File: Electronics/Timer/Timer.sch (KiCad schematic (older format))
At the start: 13 parts, among them J1 RJ12-UNSHLD, U1 74HC165

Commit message: Updated Timer schematic and updated PCB footprints
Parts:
- removed D2: D, Diodes_THT:D_A-405_P5.08mm_Vertical_AnodeUp, symbol D
- added C3: 270pF, Capacitors_SMD:C_0603_HandSoldering, symbol C
- added D2, D3, D4: D_Zener, Diodes_SMD:SOD-80C, symbol D_Zener
- added R2: 10, Resistors_SMD:R_1206_HandSoldering, symbol R
- added R3, R4: 470, Resistors_SMD:R_1206_HandSoldering, symbol R
- C1: value C -> 270pF; footprint Capacitors_THT:C_Disc_D4.3mm_W1.9mm_P5.00mm -> Capacitors_SMD:C_0603_HandSoldering
- C2: value CP1 -> 10uF; footprint Capacitors_THT:CP_Axial_L10.0mm_D6.0mm_P15.00mm_Horizontal -> Capacitors_SMD:C_1210_HandSoldering
- R1: value R -> 68; footprint Resistors_THT:R_Axial_DIN0309_L9.0mm_D3.2mm_P2.54mm_Vertical -> Resistors_SMD:R_1206_HandSoldering
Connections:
- wire segments 45 -> 57
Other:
- moved on the sheet: C2, D1, J1, R1

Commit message: Updated Timer PCB and exported GERBERS
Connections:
- net at RN1.2 (R1), U1.11 (A): now also S2.1 (Com1); no longer S1.1 (Com1)
- net at RN1.3 (R2), U1.12 (B): now also S3.1 (Com1); no longer S2.1 (Com1)
- net at RN1.4 (R3), U1.13 (C): now also S4.1 (Com1); no longer S3.1 (Com1)
- net at RN1.5 (R4), U1.14 (D): now also S5.1 (Com1); no longer S4.1 (Com1)
- net at RN1.6 (R5), U1.6 (H): now also S1.1 (Com1); no longer S5.1 (Com1)
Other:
- moved on the sheet: S1, S2, S3, S4, S5
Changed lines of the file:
@@
 L DPDT-Button S1
 U 1 1 5B2D9B30
+P 3300 5300
+F 0 "S1" H 3300 5750 60  0000 C CNN
+F 1 "DPDT-Button" H 3300 5300 60  0000 C CNN
+F 2 "PiKwonDo:Switch-DPDT" H 3300 5300 60  0001 C CNN
+F 3 "" H 3300 5300 60  0001 C CNN
+	1    3300 5300
+	1    0    0    -1
+$EndComp
+$Comp
+L DPDT-Button S2
+U 1 1 5B2D9E5E
 P 3300 1700
-F 0 "S1" H 3300 2150 60  0000 C CNN
+F 0 "S2" H 3300 2150 60  0000 C CNN
 F 1 "DPDT-Button" H 3300 1700 60  0000 C CNN
 F 2 "PiKwonDo:Switch-DPDT" H 3300 1700 60  0001 C CNN
@@
 $EndComp
 $Comp
-L DPDT-Button S2
-U 1 1 5B2D9E5E
+L DPDT-Button S3
+U 1 1 5B2D9EA4
 P 3300 2600
-F 0 "S2" H 3300 3050 60  0000 C CNN
+F 0 "S3" H 3300 3050 60  0000 C CNN
 F 1 "DPDT-Button" H 3300 2600 60  0000 C CNN
 F 2 "PiKwonDo:Switch-DPDT" H 3300 2600 60  0001 C CNN
@@
 $EndComp
 $Comp
-L DPDT-Button S3
-U 1 1 5B2D9EA4
+L DPDT-Button S4
+U 1 1 5B2D9EFB
 P 3300 3500
-F 0 "S3" H 3300 3950 60  0000 C CNN
+F 0 "S4" H 3300 3950 60  0000 C CNN
 F 1 "DPDT-Button" H 3300 3500 60  0000 C CNN
 F 2 "PiKwonDo:Switch-DPDT" H 3300 3500 60  0001 C CNN
@@
 $EndComp
 $Comp
-L DPDT-Button S4
-U 1 1 5B2D9EFB
+L DPDT-Button S5
+U 1 1 5B2D9F4B
 P 3300 4400
-F 0 "S4" H 3300 4850 60  0000 C CNN
+F 0 "S5" H 3300 4850 60  0000 C CNN
 F 1 "DPDT-Button" H 3300 4400 60  0000 C CNN
 F 2 "PiKwonDo:Switch-DPDT" H 3300 4400 60  0001 C CNN
@@
 	1    0    0    -1
 $EndComp
-$Comp
-L DPDT-Button S5
-U 1 1 5B2D9F4B
-P 3300 5300
-F 0 "S5" H 3300 5750 60  0000 C CNN
-F 1 "DPDT-Button" H 3300 5300 60  0000 C CNN
-F 2 "PiKwonDo:Switch-DPDT" H 3300 5300 60  0001 C CNN
-F 3 "" H 3300 5300 60  0001 C CNN
-	1    3300 5300
-	1    0    0    -1
-$EndComp

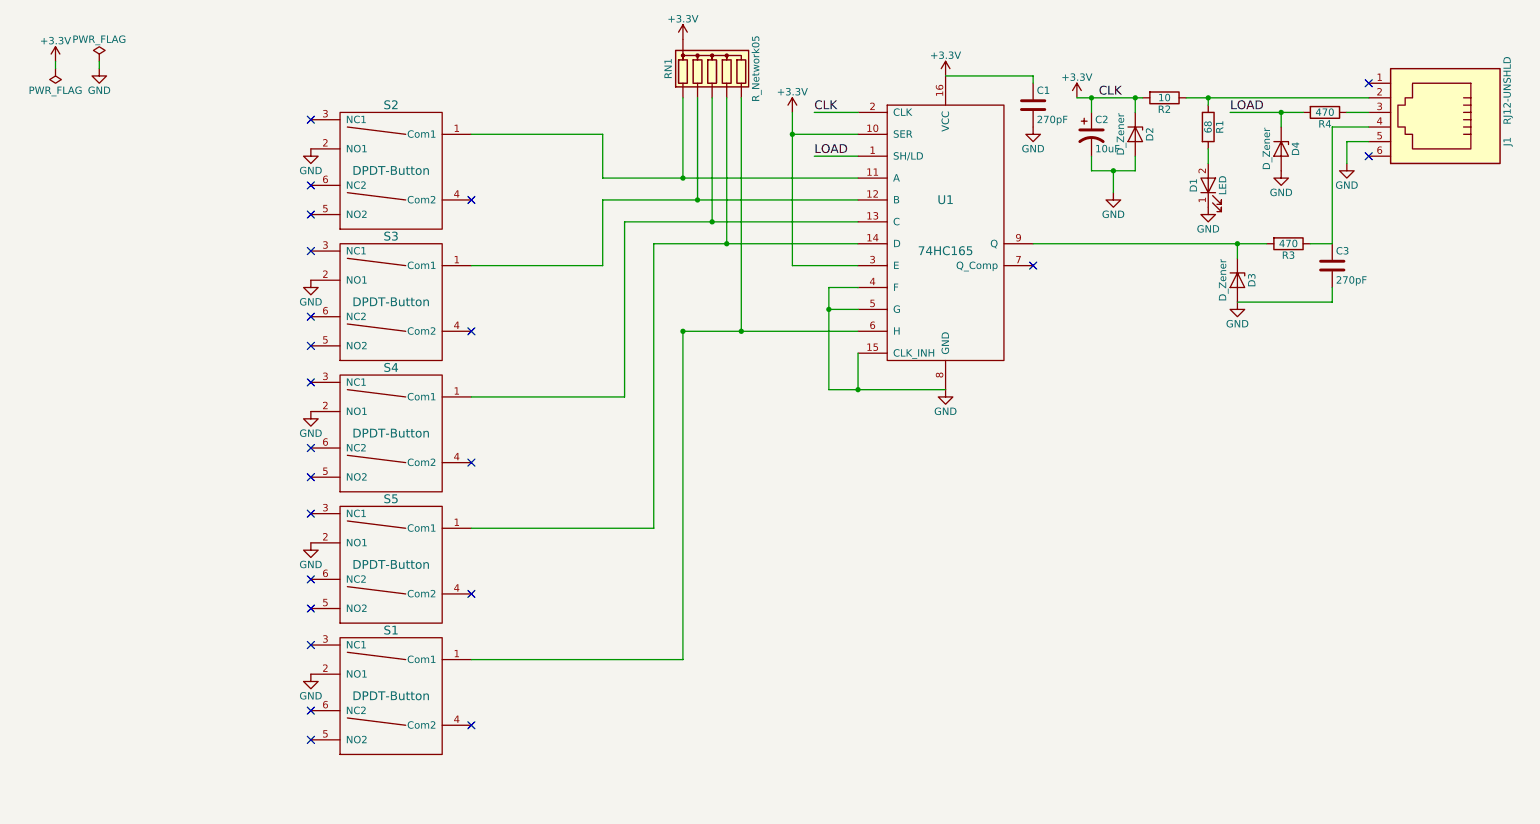
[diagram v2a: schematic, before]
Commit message: Completed HAT PCB
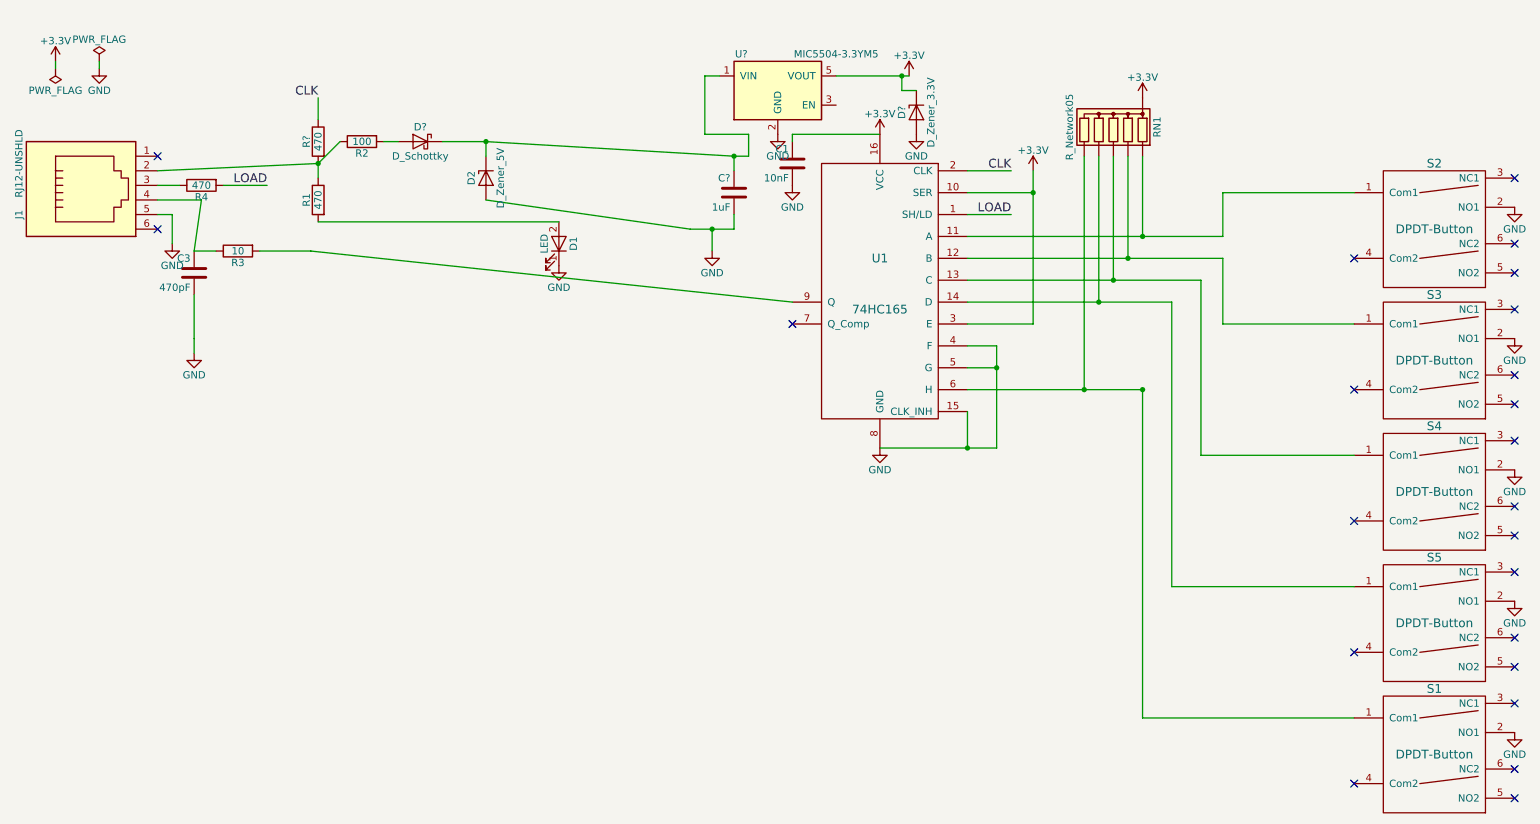
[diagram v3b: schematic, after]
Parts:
- removed C2: 10uF, Capacitors_SMD:C_1210_HandSoldering, symbol CP1
- removed D3, D4: D_Zener, Diodes_SMD:SOD-80C, symbol D_Zener
- added C?: 1uF, Capacitors_SMD:C_0603_HandSoldering, symbol C
- added D?: D_Schottky, symbol D_Schottky
- added D?: D_Zener_3.3V, Diodes_SMD:SOD-80C, symbol D_Zener
- added R?: 470, Resistors_SMD:R_1206_HandSoldering, symbol R
- added U?: MIC5504-3.3YM5, TO_SOT_Packages_SMD:SOT-23-5, symbol MIC5504-3.3YM5
- C1: value 270pF -> 10nF
- C3: value 270pF -> 470pF
- D2: value D_Zener -> D_Zener_5V
- R1: value 68 -> 470
- R2: value 10 -> 100
- R3: value 470 -> 10
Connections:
- net +3V3: now also D?.1 (K), U?.5 (VOUT); no longer D2.1 (K), R2.2, U1.2 (CLK)
- net GND: now also C?.2, D?.2 (A), U?.2 (GND)
- net at J1.2, R1.1, R2.1: now also R?.2
- new net: D?.2 (A), R2.2
- new net: C?.1, D2.1 (K), D?.1 (K), U?.1 (VIN)
- new net CLK: R?.1, U1.2 (CLK)
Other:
- moved on the sheet: C1, C3, D1, D2, J1, R1, R2, R3, R4, RN1, S1, S2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

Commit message: Updated HAT PCB footprints and BOM
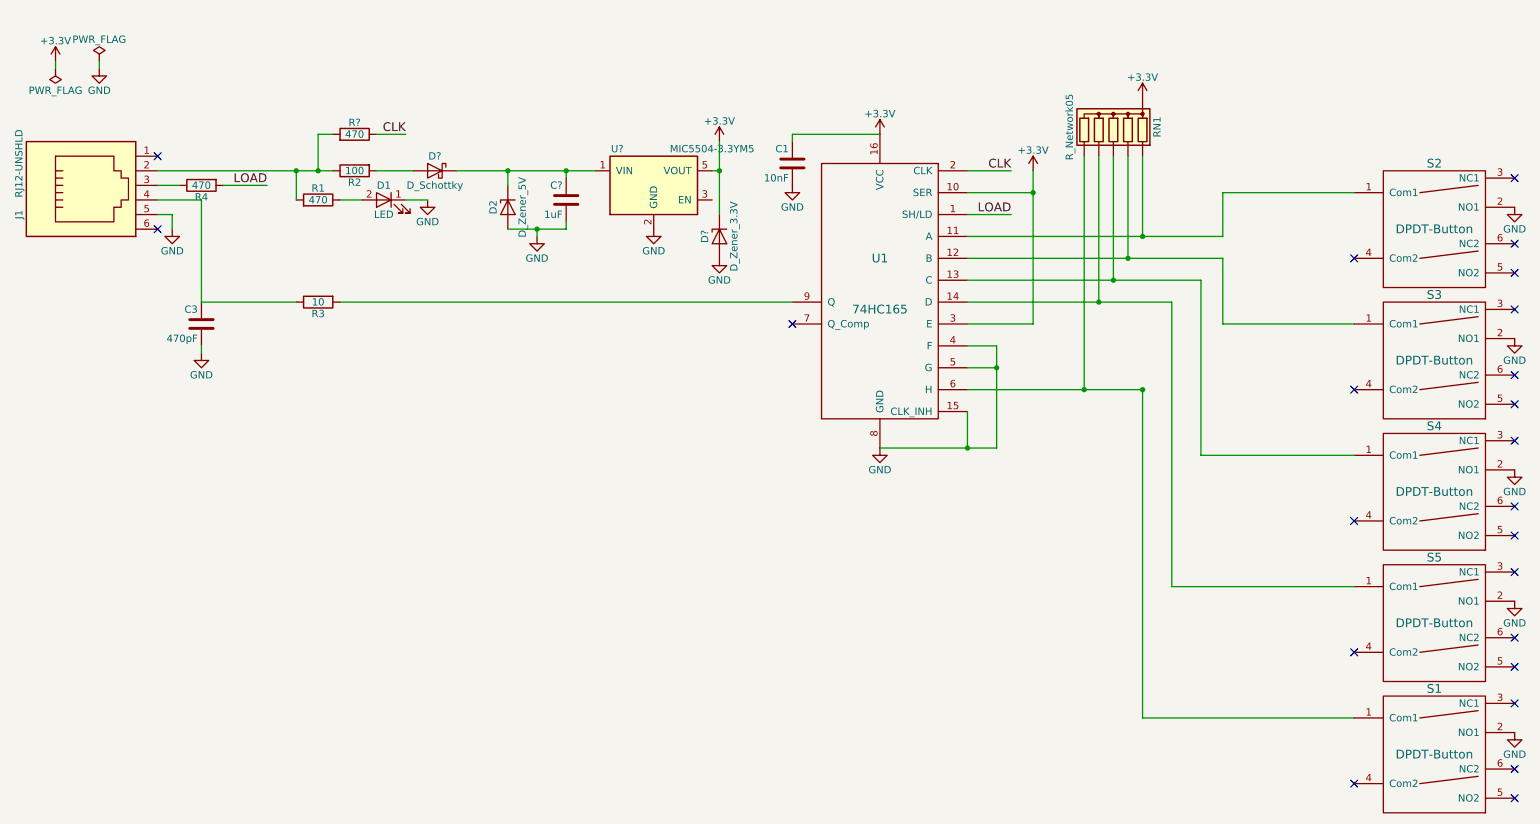
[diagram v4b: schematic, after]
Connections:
- net at J1.2, R2.1, R?.2: now also R1.2; no longer R1.1
- net at D1.2 (A): now also R1.1; no longer R1.2
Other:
- moved on the sheet: C3, C?, D1, D2, D?, R2, R3, R?, U?

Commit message: Updated Timer schematic, footprints, BOM, and PCB
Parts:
- C1: footprint Capacitors_SMD:C_0603_HandSoldering -> Capacitors_SMD:C_0805_HandSoldering
- C2: renamed from C?; footprint Capacitors_SMD:C_0603_HandSoldering -> Capacitors_SMD:C_1206_HandSoldering
- C3: footprint Capacitors_SMD:C_0603_HandSoldering -> Capacitors_SMD:C_1206_HandSoldering
- D2: footprint Diodes_SMD:SOD-80C -> Diodes_SMD:D_SOD-323_HandSoldering
- D3: renamed from D?; footprint (none) -> Diodes_SMD:D_SOD-123
- D4: renamed from D?; footprint Diodes_SMD:SOD-80C -> Diodes_SMD:D_SOD-323_HandSoldering
- gave numbers to parts that had none: 2
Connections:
- net +3V3: no longer U1.10 (SER)
- net GND: now also U1.10 (SER)
- net PWR-CLK-IN: now reaches J1.2, R1.2, R2.1, R5.2
- net Q-Out: now reaches C3.1, J1.4, R3.1
- net Q: now reaches R3.2, U1.9 (Q)
- net 5V-In: now reaches C2.1, D2.1 (K), D3.1 (K), U2.1 (VIN)
- net 5V-In: now also U2.3 (EN)

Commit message: Revert "Merge branch 'master' into electronics-tweaks; overwrite 'master' hat changes"
This reverts commit 8490e2c3782f3b2eaf596155d8884dc6cd65858c, reversing
changes made to 143268d8e254d2edd056497eb53e137ee58f0f7c.
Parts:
- C1: footprint Capacitors_SMD:C_0805_HandSoldering -> Capacitors_SMD:C_0603_HandSoldering
- C3: footprint Capacitors_SMD:C_1206_HandSoldering -> Capacitors_SMD:C_0603_HandSoldering
- C?: renamed from C2; footprint Capacitors_SMD:C_1206_HandSoldering -> Capacitors_SMD:C_0603_HandSoldering
- D2: footprint Diodes_SMD:D_SOD-323_HandSoldering -> Diodes_SMD:SOD-80C
- D?: renamed from D3; footprint Diodes_SMD:D_SOD-123 -> (none)
- D?: renamed from D4; footprint Diodes_SMD:D_SOD-323_HandSoldering -> Diodes_SMD:SOD-80C
- renumbered R5 to R?, U2 to U?
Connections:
- net +3V3: now also U1.10 (SER)
- net GND: no longer U1.10 (SER)
- net at R1.1: now also J1.2, R2.1, R?.2; no longer D1.2 (A)
- net 5V-In: no longer names the net of C?.1, D2.1 (K), D?.1 (K), U?.1 (VIN)
- net 5V-In: no longer U?.3 (EN)
- removed net PWR-CLK-IN: J1.2, R1.2, R2.1, R?.2
- net Q: no longer names the net of R3.2, U1.9 (Q)
- net Q-Out: no longer names the net of C3.1, J1.4, R3.1
- new net: D1.2 (A), R1.2
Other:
- moved on the sheet: C3, C?, D1, D2, D?, R2, R3, R?, U?

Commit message: Timer: Restore David's updated schematic and PCB from earlier failed merge.
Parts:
- C1: footprint Capacitors_SMD:C_0603_HandSoldering -> Capacitors_SMD:C_0805_HandSoldering
- C2: renamed from C?; footprint Capacitors_SMD:C_0603_HandSoldering -> Capacitors_SMD:C_1206_HandSoldering
- C3: footprint Capacitors_SMD:C_0603_HandSoldering -> Capacitors_SMD:C_1206_HandSoldering
- D2: footprint Diodes_SMD:SOD-80C -> Diodes_SMD:D_SOD-323_HandSoldering
- D3: renamed from D?; footprint (none) -> Diodes_SMD:D_SOD-123
- D4: renamed from D?; footprint Diodes_SMD:SOD-80C -> Diodes_SMD:D_SOD-323_HandSoldering
- gave numbers to parts that had none: 2
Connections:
- net +3V3: no longer U1.10 (SER)
- net GND: now also U1.10 (SER)
- net PWR-CLK-IN: now reaches J1.2, R2.1, R5.2
- net PWR-CLK-IN: now also R1.2; no longer R1.1
- net Q-Out: now reaches C3.1, J1.4, R3.1
- net Q: now reaches R3.2, U1.9 (Q)
- net at D1.2 (A): now also R1.1; no longer R1.2
- net 5V-In: now reaches C2.1, D2.1 (K), D3.1 (K), U2.1 (VIN)
- net 5V-In: now also U2.3 (EN)
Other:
- moved on the sheet: C2, C3, D1, D2, D3, D4, R2, R3, R5, U2

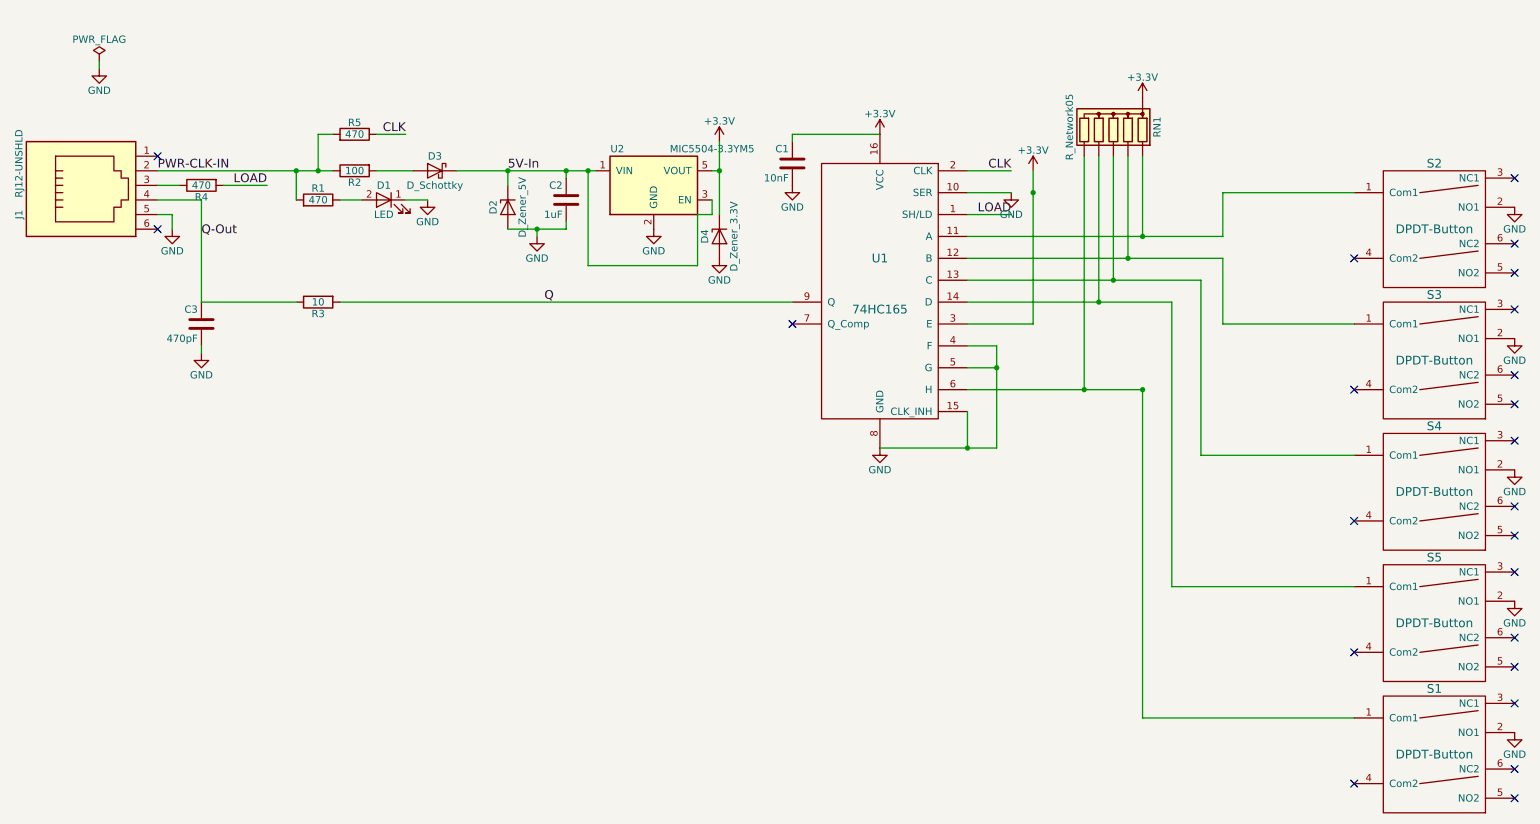
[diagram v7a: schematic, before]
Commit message: Timer: Cleaned up schematic; reassigned reference numbers.
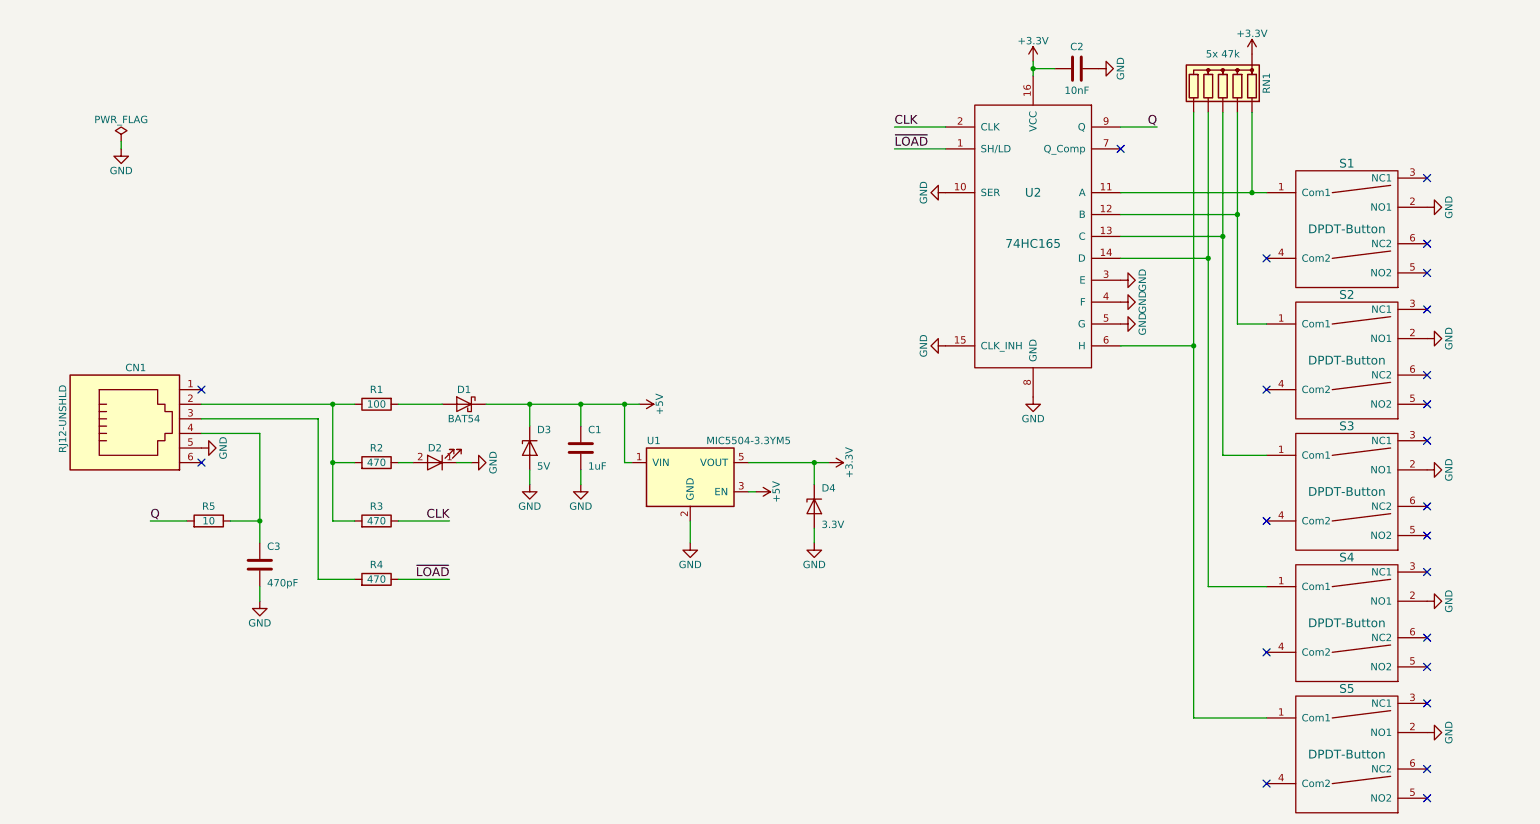
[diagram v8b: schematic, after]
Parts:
- removed R1: 470, Resistors_SMD:R_1206_HandSoldering, symbol R
- removed U1: 74HC165, Housings_DIP:DIP-16_W7.62mm, symbol 74HC165
- added R5: 10, Resistors_SMD:R_1206_HandSoldering, symbol R
- added U2: 74HC165, symbol 74HC165_PKD
- D1: renamed from D3; value D_Schottky -> BAT54
- D3: renamed from D2; value D_Zener_5V -> 5V
- D4: value D_Zener_3.3V -> 3.3V
- R3: value 10 -> 470
- RN1: value R_Network05 -> 5x 47k
- renumbered C2 to C1, C1 to C2, J1 to CN1, D1 to D2, R2 to R1, R5 to R2, S2 to S1, S3 to S2, S4 to S3, S5 to S4, S1 to S5, U2 to U1
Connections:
- net LOAD is gone; now on an unnamed net: R4.2
- net +3V3: now also C2.2, U2.16 (VCC); no longer C2.1
- net CLK: now also R3.1, U2.2 (CLK); no longer R2.1
- net GND: now also C2.1, U2.10 (SER), U2.15 (CLK_INH), U2.3 (E), U2.4 (F), U2.5 (G), U2.8 (GND); no longer C2.2
- net Q: now also R5.2, U2.9 (Q); no longer R3.2
- net at RN1.2 (R1), S1.1 (Com1): now also U2.11 (A)
- net at RN1.3 (R2), S2.1 (Com1): now also U2.12 (B)
- net at RN1.4 (R3), S3.1 (Com1): now also U2.13 (C)
- net at RN1.5 (R4), S4.1 (Com1): now also U2.14 (D)
- net at RN1.6 (R5), S5.1 (Com1): now also U2.6 (H)
- net at CN1.3: no longer R4.1
- net at D2.2 (A): now also R2.1
- net 5V-In renamed +5V
- net PWR-CLK-IN: no longer names the net of CN1.2, R1.1, R2.2
- net PWR-CLK-IN: now also R3.2
- net Q-Out: no longer names the net of C3.1, CN1.4
- net Q-Out: now also R5.1; no longer R3.1
- new net ~LOAD~: R4.1, U2.1 (SH/LD)
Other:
- moved on the sheet: C1, C2, CN1, D1, D2, D3, R1, R2, RN1, S1, S2, S3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
